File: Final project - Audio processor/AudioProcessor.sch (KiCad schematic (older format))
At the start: 77 parts, among them J1 INPUT STEREO, J2 INPUT MONO STEREO, J3 JCH1, J4 JCH2, J5 ALIMENTACION, J6 JCH3, J7 OUTPUT STEREO, J8 OUTPUT MONO STEREO, J9 I2C & RS232 CONNECTOR, Q1 Q_NPN_BCE, Q2 Q, Q3 Q_NPN_BCE, Q4 Q_NPN_BCE, U1 LM2904, U2 LM2904, U3 pcm5100

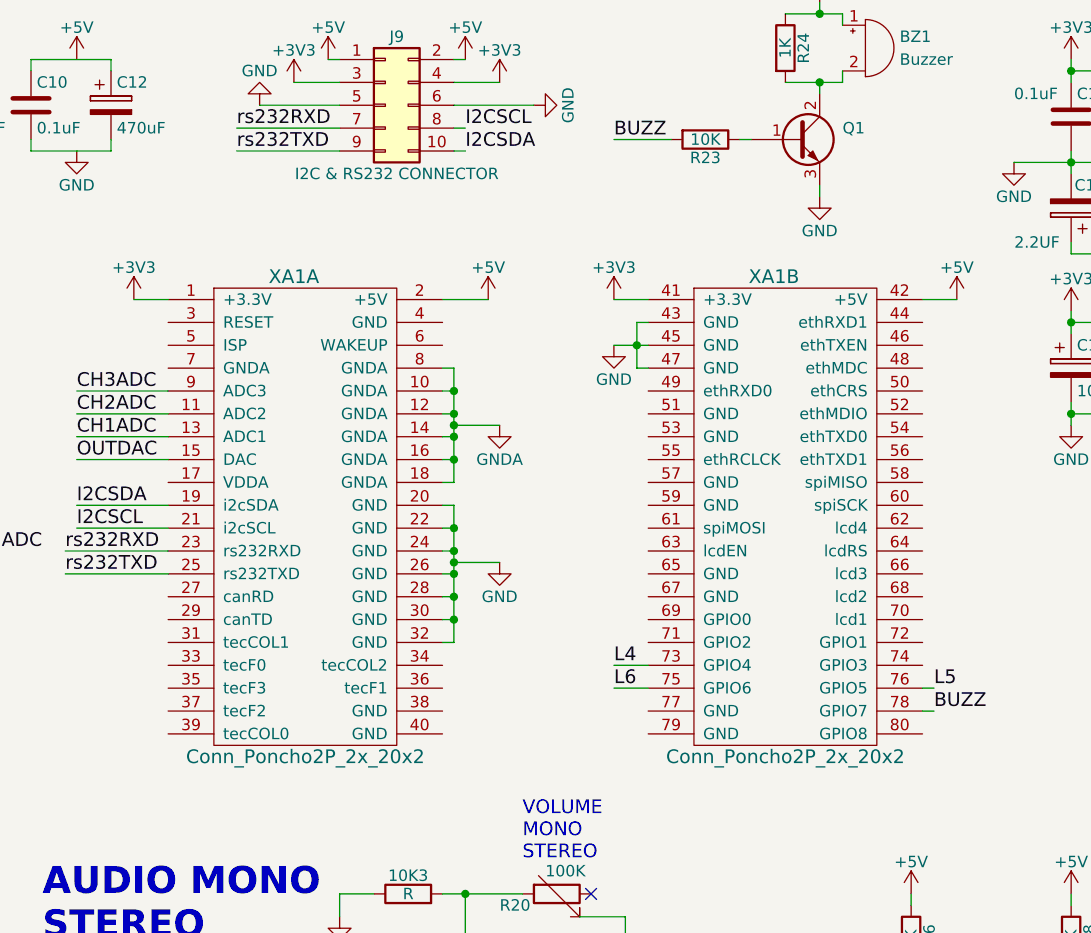
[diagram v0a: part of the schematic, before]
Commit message: Se actualiza el esquematico
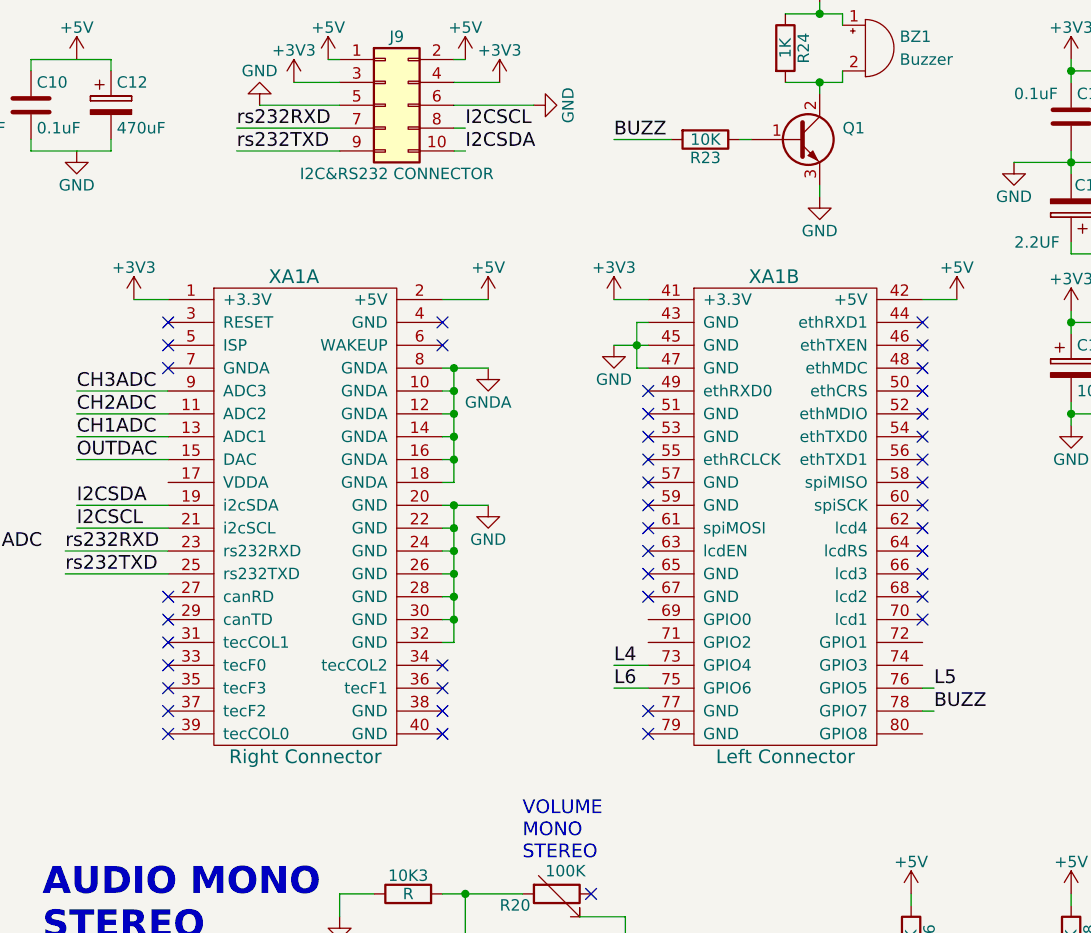
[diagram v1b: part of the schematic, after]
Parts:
- J9: value I2C & RS232 CONNECTOR -> I2C&RS232 CONNECTOR
- XA1: value Conn_Poncho2P_2x_20x2 -> Right Connector
- XA1: value Conn_Poncho2P_2x_20x2 -> Left Connector
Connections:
- no-connect marks 3 -> 45
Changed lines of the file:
@@
 P 4600 2400
 F 0 "XA1" H 4900 2800 60  0000 C CNN
-F 1 "Conn_Poncho2P_2x_20x2" H 4950 700 60  0000 C CNN
+F 1 "Right Connector" H 4950 700 60  0000 C CNN
 F 2 "" H 4600 2400 60  0000 C CNN
 F 3 "" H 4600 2400 60  0000 C CNN
@@
 P 6700 2400
 F 0 "XA1" H 7000 2800 60  0000 C CNN
-F 1 "Conn_Poncho2P_2x_20x2" H 7050 700 60  0000 C CNN
+F 1 "Left Connector" H 7050 700 60  0000 C CNN
 F 2 "" H 6700 2400 60  0000 C CNN
 F 3 "" H 6700 2400 60  0000 C CNN
@@
 L GNDA #PWR36
 U 1 1 5BA0895E
-P 5800 2650
-F 0 "#PWR36" H 5800 2400 50  0001 C CNN
-F 1 "GNDA" H 5800 2500 50  0000 C CNN
-F 2 "" H 5800 2650 50  0001 C CNN
-F 3 "" H 5800 2650 50  0001 C CNN
-	1    5800 2650
+P 5750 2400
+F 0 "#PWR36" H 5750 2150 50  0001 C CNN
+F 1 "GNDA" H 5750 2250 50  0000 C CNN
+F 2 "" H 5750 2400 50  0001 C CNN
+F 3 "" H 5750 2400 50  0001 C CNN
+	1    5750 2400
 	1    0    0    -1
 $EndComp
@@
 L GND #PWR37
 U 1 1 5BA0ECD7
-P 5800 3250
-F 0 "#PWR37" H 5800 3000 50  0001 C CNN
-F 1 "GND" H 5800 3100 50  0000 C CNN
-F 2 "" H 5800 3250 50  0001 C CNN
-F 3 "" H 5800 3250 50  0001 C CNN
-	1    5800 3250
+P 5750 3000
+F 0 "#PWR37" H 5750 2750 50  0001 C CNN
+F 1 "GND" H 5750 2850 50  0000 C CNN
+F 2 "" H 5750 3000 50  0001 C CNN
+F 3 "" H 5750 3000 50  0001 C CNN
+	1    5750 3000
 	1    0    0    -1
 $EndComp
@@
 $EndComp
 Wire Wire Line
-	5550 3000 5600 3000
+	5550 3000 5750 3000
 Wire Wire Line
 	5600 3000 5600 3600
@@
 	5550 3100 5600 3100
 Connection ~ 5600 3100
-Wire Wire Line
-	5800 3250 5600 3250
-Connection ~ 5600 3250
 Wire Wire Line
 	6450 2300 6300 2300
@@
 	3950 3100 4350 3100
 Wire Wire Line
-	5600 2400 5550 2400
+	5550 2400 5750 2400
 Connection ~ 5600 2500
 $Comp
@@
 P 5300 1250
 F 0 "J9" H 5350 1550 50  0000 C CNN
-F 1 "I2C & RS232 CONNECTOR" H 5350 950 50  0000 C CNN
+F 1 "I2C&RS232 CONNECTOR" H 5350 950 50  0000 C CNN
 F 2 "" H 5300 1250 50  0001 C CNN
 F 3 "" H 5300 1250 50  0001 C CNN
@@
 Wire Wire Line
 	5550 2700 5600 2700
-Wire Wire Line
-	5600 2650 5800 2650
-Connection ~ 5600 2650
 Text Label 6300 1400 0    60   ~ 0
 BUZZ
@@
 	7200 800  7200 850
 Connection ~ 7200 850
+NoConn ~ 4350 3400
+NoConn ~ 4350 3500
+NoConn ~ 4350 3600
+NoConn ~ 4350 3700
+NoConn ~ 4350 3800
+NoConn ~ 4350 3900
+NoConn ~ 4350 4000
+NoConn ~ 5550 3800
+NoConn ~ 5550 3700
+NoConn ~ 5550 4000
+NoConn ~ 5550 3900
+NoConn ~ 7650 2600
+NoConn ~ 7650 2200
+NoConn ~ 7650 2300
+NoConn ~ 7650 2400
+NoConn ~ 7650 2500
+NoConn ~ 7650 2700
+NoConn ~ 7650 2800
+NoConn ~ 7650 2900
+NoConn ~ 7650 3000
+NoConn ~ 6450 2500
+NoConn ~ 6450 2600
+NoConn ~ 6450 2700
+NoConn ~ 6450 2800
+NoConn ~ 6450 2900
+NoConn ~ 6450 3000
+NoConn ~ 6450 3100
+NoConn ~ 6450 3200
+NoConn ~ 7650 3100
+NoConn ~ 7650 3200
+NoConn ~ 7650 3300
+NoConn ~ 7650 3400
+NoConn ~ 7650 3500
+NoConn ~ 6450 3300
+NoConn ~ 6450 3400
+NoConn ~ 6450 3900
+NoConn ~ 6450 4000
+NoConn ~ 5550 2200
+NoConn ~ 5550 2300
+Connection ~ 5600 2400
+Connection ~ 5600 3000
+NoConn ~ 4350 2400
+NoConn ~ 4350 2300
+NoConn ~ 4350 2200
 $EndSCHEMATC

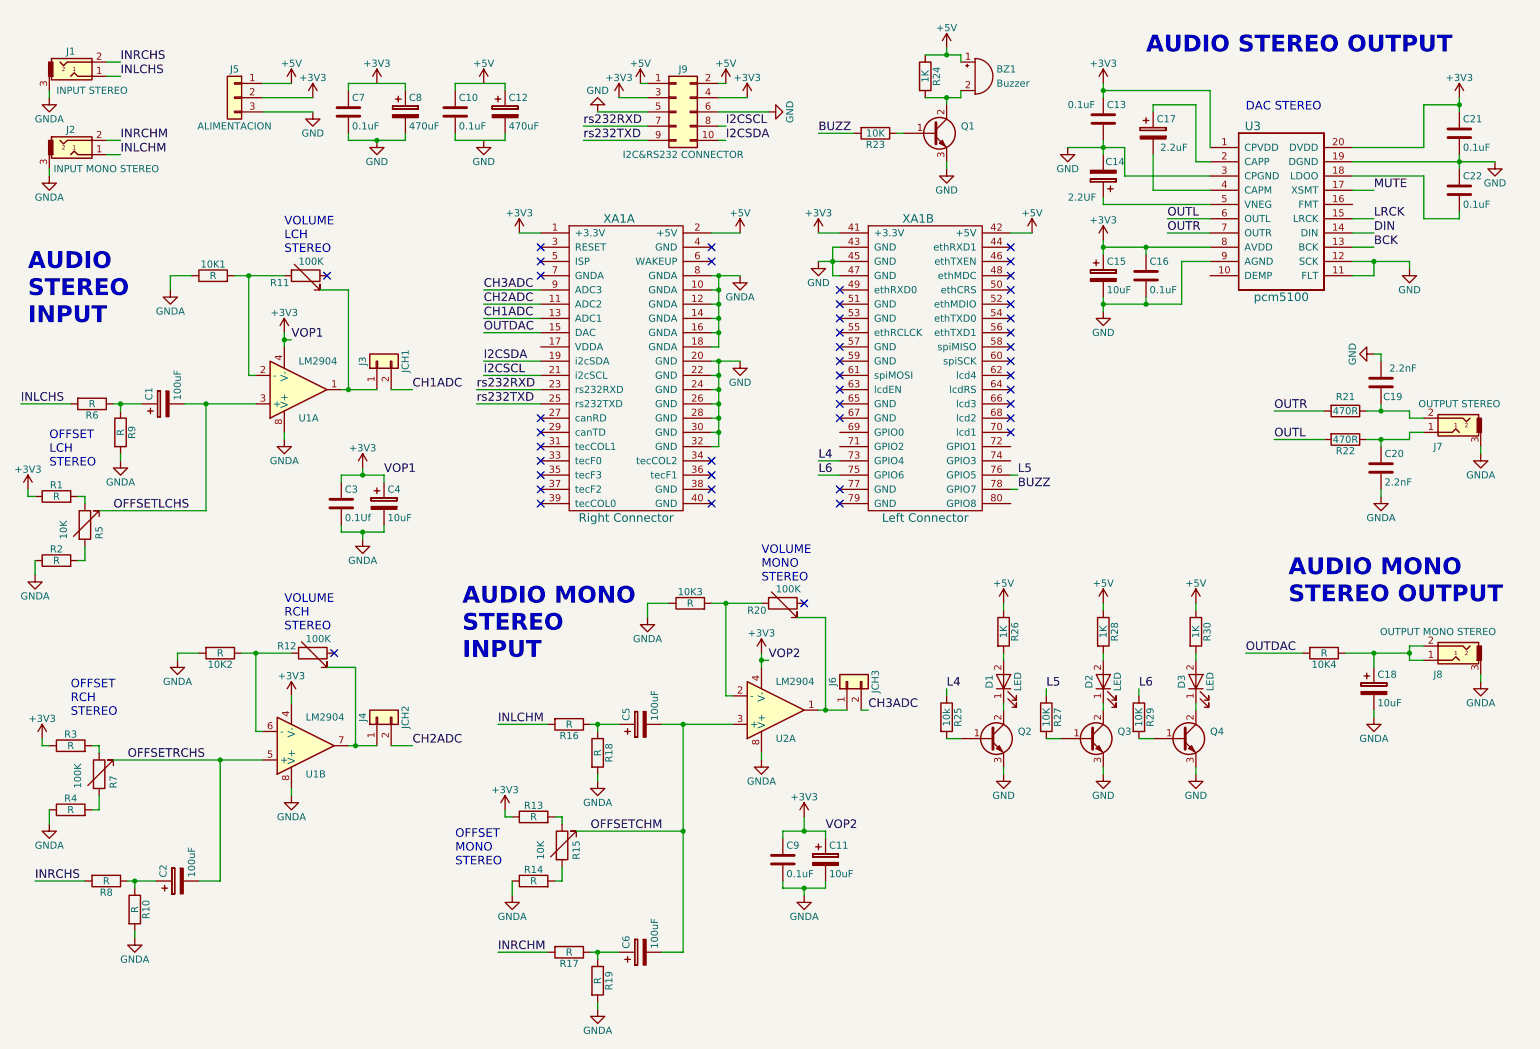
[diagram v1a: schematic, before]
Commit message: Se actualizo el esquematico
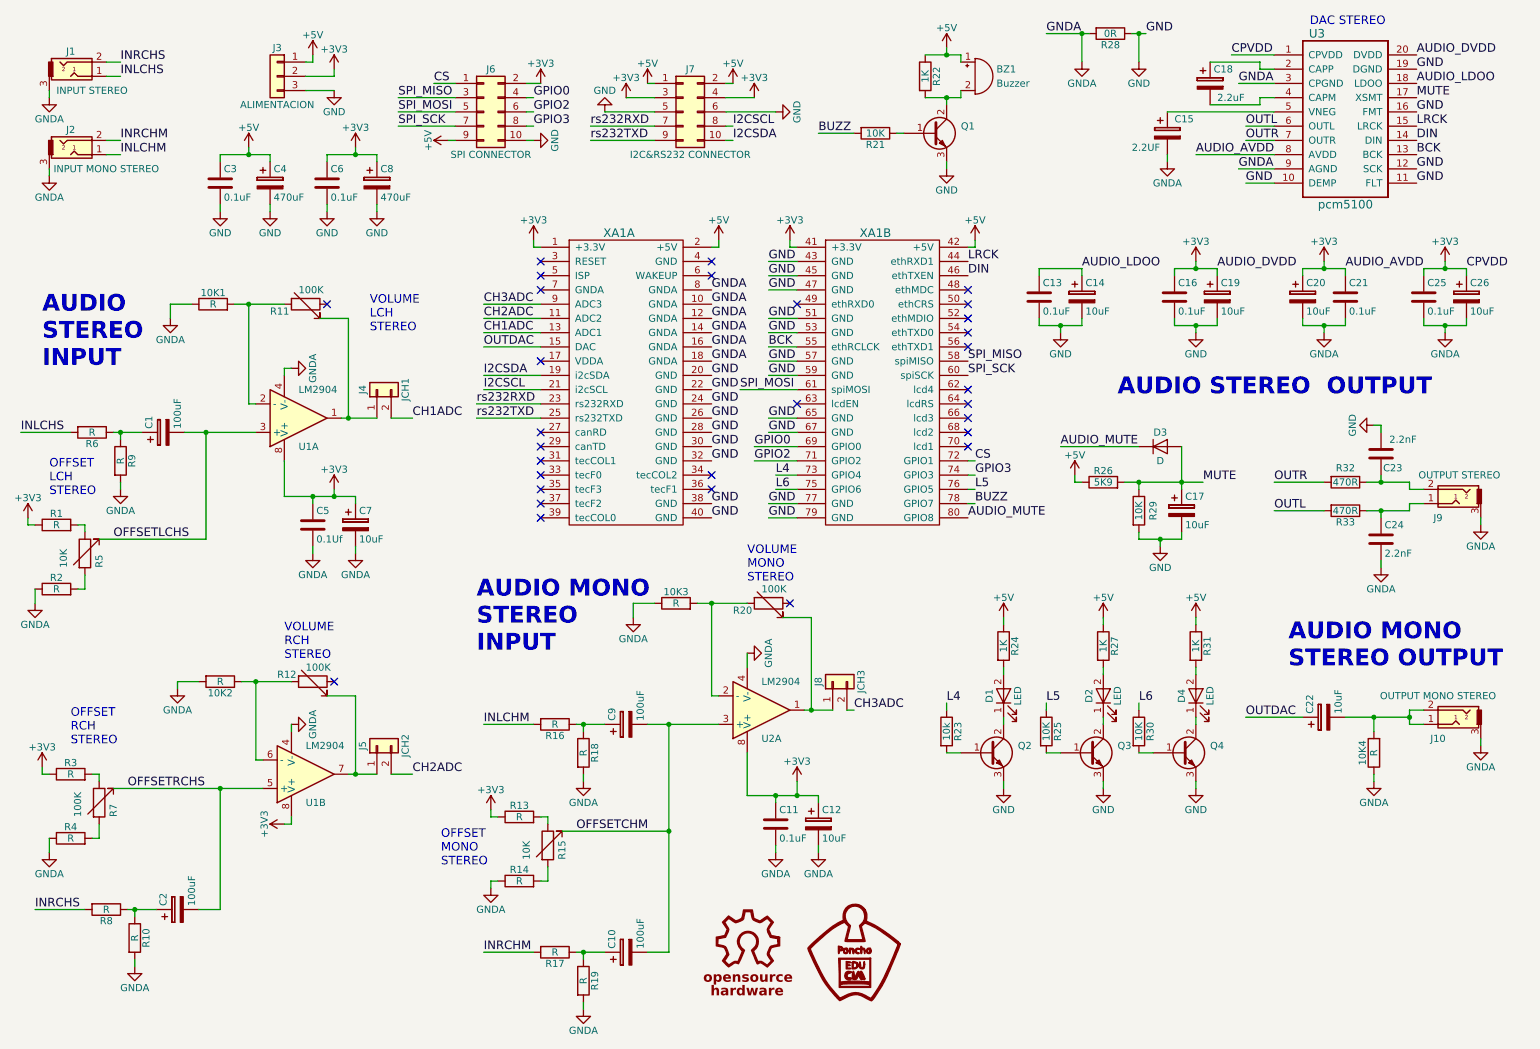
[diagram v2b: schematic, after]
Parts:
- removed C13: 0.1uF, symbol C
- added C14, C17, C19, C26: 10uF, symbol CP
- added C25: 0.1uF, symbol C
- added D3: D, symbol D
- added J6: SPI CONNECTOR, symbol Conn_02x05_Odd_Even
- added R26: 5K9, symbol R
- added R28: 0R, symbol R
- added R29: 10K, symbol R
- XA1: value Right Connector -> Conn_Poncho2P_2x_20x2
- XA1: value Left Connector -> Conn_Poncho2P_2x_20x2
- renumbered C6 to C10, C9 to C11, C11 to C12, C22 to C13, C14 to C15, C21 to C16, C17 to C18, C15 to C20, C16 to C21, C18 to C22, C19 to C23, C20 to C24, C10 to C3, C12 to C4, C3 to C5, C7 to C6, C4 to C7, C5 to C9, D3 to D4, J8 to J10, J5 to J3, J3 to J4, J4 to J5, J9 to J7, J6 to J8, J7 to J9, R23 to R21, R24 to R22, R25 to R23, R26 to R24, R27 to R25, R28 to R27, R29 to R30, R30 to R31, R21 to R32, R22 to R33
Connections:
- net +3V3: now also C6.1, C8.1, U1.8 (V+), U1.8 (V+), U2.8 (V+), C19.1, C25.1, C26.1, J6.2 (Pin_2); no longer U1.4 (V-), U1.4 (V-), U2.4 (V-)
- net +5V: now also C3.1, C4.1, J6.9 (Pin_9), R26.1
- net BCK: now also XA1.55 (ethRCLCK)
- net DIN: now also XA1.46 (ethTXEN)
- net GND: now also C13.2, C3.2, C4.2, U3.10 (DEMP), U3.16 (FMT), XA1.38 (GND), XA1.40 (GND), XA1.51 (GND), XA1.53 (GND), XA1.57 (GND), XA1.59 (GND), XA1.65 (GND), XA1.67 (GND), XA1.77 (GND), XA1.79 (GND), C14.2, C17.2, C19.2, J6.10 (Pin_10), R28.1, R29.2; no longer C13.1, C15.2, C20.2, C21.2, U3.3 (CPGND), U3.9 (AGND)
- net GNDA: now also 10K4.1, C15.2, C20.2, C21.2, U1.4 (V-), U1.4 (V-), U2.4 (V-), U3.3 (CPGND), U3.9 (AGND), C25.2, C26.2, R28.2; no longer C22.2, U1.8 (V+), U1.8 (V+), U2.8 (V+)
- net LRCK: now also XA1.44 (ethRXD1)
- net MUTE: now also C17.1, D3.2 (A), R26.2, R29.1
- net OUTDAC: now also C22.1; no longer 10K4.2
- net AUDIO_LDOO: now reaches U3.18 (LDOO)
- net AUDIO_LDOO: now also C13.1, C14.1; no longer C13.2
- net at J10.1, J10.2: now also 10K4.2, C22.2; no longer 10K4.1, C22.1
- net SPI_MISO: now reaches XA1.58 (spiMISO)
- net SPI_MISO: now also J6.3 (Pin_3)
- net SPI_SCK: now reaches XA1.60 (spiSCK)
- net SPI_SCK: now also J6.7 (Pin_7)
- net SPI_MOSI: now reaches XA1.61 (spiMOSI)
- net SPI_MOSI: now also J6.5 (Pin_5)
- net GPIO0: now reaches XA1.69 (GPIO0)
- net GPIO0: now also J6.4 (Pin_4)
- net GPIO2: now reaches XA1.71 (GPIO2)
- net GPIO2: now also J6.6 (Pin_6)
- net CS: now reaches XA1.72 (GPIO1)
- net CS: now also J6.1 (Pin_1)
- net GPIO3: now reaches XA1.74 (GPIO3)
- net GPIO3: now also J6.8 (Pin_8)
- net AUDIO_MUTE: now reaches XA1.80 (GPIO8)
- net AUDIO_MUTE: now also D3.1 (K)
- no-connect marks 45 -> 30
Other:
- moved on the sheet: 10K1, 10K2, 10K3, 10K4, C1, C10, C11, C12, C13, C15, C16, C18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

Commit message: Actualizacion repo
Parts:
- BZ1: footprint (none) -> Buzzers_Beepers:Buzzer_12x9.5RM7.6
- C1, C10, C2, C9: footprint (none) -> Capacitors_SMD:CP_Elec_6.3x5.3
- C11, C13, C16, C21, C23, C24, C25, C3, C5, C6: footprint (none) -> Capacitors_SMD:C_1206_HandSoldering
- C12, C14, C17, C19, C20, C22, C26, C7: footprint (none) -> Capacitors_SMD:CP_Elec_5x5.3
- C15, C18: footprint (none) -> Capacitors_THT:CP_Radial_D5.0mm_P2.50mm
- C4, C8: footprint (none) -> Capacitors_THT:CP_Radial_D10.0mm_P5.00mm
- D1, D2, D4: footprint (none) -> LEDs:LED_1206_HandSoldering
- D3: value D -> 1N4148; footprint (none) -> Diodes_SMD:D_1206
- J1, J10, J2, J9: footprint (none) -> Connectors:BARREL_JACK
- J3: footprint (none) -> TerminalBlocks_Phoenix:TerminalBlock_Phoenix_MKDS1.5-3pol
- J4, J5, J8: footprint (none) -> Pin_Headers:Pin_Header_Straight_1x02_Pitch2.54mm
- J6: value SPI CONNECTOR -> SPI & I/0; footprint (none) -> Socket_Strips:Socket_Strip_Straight_2x05_Pitch2.54mm
- J7: value I2C&RS232 CONNECTOR -> I2C & RS232; footprint (none) -> Socket_Strips:Socket_Strip_Straight_2x05_Pitch2.54mm
- Q1, Q2, Q3, Q4: footprint (none) -> TO_SOT_Packages_THT:TO-92_Molded_Narrow
- R1, R13, R14, R2, R3, R4: value R -> 1K; footprint (none) -> Resistors_SMD:R_1206_HandSoldering
- R10, R16, R17, R18, R19, R6, R8, R9: value R -> 10K; footprint (none) -> Resistors_SMD:R_2010_HandSoldering
- R11, R12, R15, R20, R5: footprint (none) -> Potentiometers:Potentiometer_Trimmer_Bourns_3296W
- R21, R23, R25, R29, R30: footprint (none) -> Resistors_SMD:R_2010_HandSoldering
- R22, R24, R26, R27, R28, R31, R32, R33: footprint (none) -> Resistors_SMD:R_1206_HandSoldering
- R34: renamed from 10K1; value R -> 10K; footprint (none) -> Resistors_SMD:R_2010_HandSoldering
- R35: renamed from 10K2; value R -> 10K; footprint (none) -> Resistors_SMD:R_2010_HandSoldering
- R36: renamed from 10K3; value R -> 10K; footprint (none) -> Resistors_SMD:R_2010_HandSoldering
- R37: renamed from 10K4; value R -> 10K; footprint (none) -> Resistors_SMD:R_2010_HandSoldering
- R7: value 100K -> 10K; footprint (none) -> Potentiometers:Potentiometer_Trimmer_Bourns_3296W
- U1, U2: footprint (none) -> Housings_SOIC:SOIC-8_3.9x4.9mm_Pitch1.27mm
- U3: footprint (none) -> Housings_SSOP:TSSOP-20_4.4x6.5mm_Pitch0.65mm
- XA1: footprint (none) -> Poncho_Esqueleto:Conn_Poncho_Completo
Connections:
- net +3V3: no longer XA1.1 (+3.3V)
- net +5V: no longer XA1.2 (+5V)
- no-connect marks 30 -> 32

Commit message: Se actualiza el PCB, todavia queda rutear un poco.
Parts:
- removed BZ1: Buzzer, Buzzers_Beepers:Buzzer_12x9.5RM7.6, symbol Buzzer
- removed Q1: Q_NPN_BCE, TO_SOT_Packages_THT:TO-92_Molded_Narrow, symbol Q_NPN_BCE
- removed R21: 10K, Resistors_SMD:R_2010_HandSoldering, symbol R
- removed R22: 1K, Resistors_SMD:R_1206_HandSoldering, symbol R
- R11, R12, R15, R20, R5, R7: symbol R_Variable -> R_Variable-RESCUE-AudioProcessor
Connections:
- net BUZZ: no longer names the net of XA1.78 (GPIO7)
- no-connect marks 32 -> 33
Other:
- moved on the sheet: J6, J7, R28

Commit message: avanzando con el pcb
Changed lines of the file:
@@
 	7850 2400 7850 2350
 Wire Wire Line
-	8150 2350 8150 2400
-Text Label 8150 2350 0    60   ~ 0
+	8150 2250 8150 2400
+Text Label 8150 2250 0    60   ~ 0
 AUDIO_LDOO
 Text Label 10500 950  0    60   ~ 0
@@
 	8800 2350 9100 2350
 Wire Wire Line
-	9100 2350 9100 2400
+	9100 2250 9100 2400
 Wire Wire Line
 	8800 2700 8800 2750
@@
 	8950 2300 8950 2350
 Connection ~ 8950 2350
-Text Label 9100 2350 0    60   ~ 0
+Text Label 9100 2250 0    60   ~ 0
 AUDIO_DVDD
 Wire Wire Line
@@
 	9700 2350 10000 2350
 Wire Wire Line
-	10000 2350 10000 2400
+	10000 2250 10000 2400
 Wire Wire Line
 	9850 2300 9850 2350
@@
 Text Label 8950 1550 0    60   ~ 0
 AUDIO_AVDD
-Text Label 10000 2350 0    60   ~ 0
+Text Label 10000 2250 0    60   ~ 0
 AUDIO_AVDD
 Text Label 9250 1650 0    60   ~ 0
@@
 	10550 2350 10850 2350
 Wire Wire Line
-	10850 2350 10850 2400
+	10850 2250 10850 2400
 Wire Wire Line
 	10700 2300 10700 2350
@@
 Wire Wire Line
 	9500 850  9200 850
-Text Label 10850 2350 0    60   ~ 0
+Text Label 10850 2250 0    60   ~ 0
 CPVDD
 $Comp
@@
 	5900 1250 6100 1250
 NoConn ~ 7400 4000
+Connection ~ 9100 2350
+Connection ~ 8150 2350
+Connection ~ 10000 2350
+Connection ~ 10850 2350
 $EndSCHEMATC

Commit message: Version 2 del pcb del procesador de audio
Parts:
- D3: footprint Diodes_SMD:D_1206 -> Diodes_THT:D_A-405_P10.16mm_Horizontal
- R32, R33: footprint Resistors_SMD:R_1206_HandSoldering -> Resistors_THT:R_Axial_DIN0207_L6.3mm_D2.5mm_P10.16mm_Horizontal
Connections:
- net AUDIO_LDOO: no longer names the net of C13.1, C14.1, U3.18 (LDOO)
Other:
- note added: "AUDIO STEREO \nOUTPUT\n"
- note removed: "AUDIO STEREO OUTPUT\n"
- moved on the sheet: C13, C14, C15, C16, C17, C18, C19, C20, C21, C25, C26, D3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

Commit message: version Final
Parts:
- J1, J10, J2, J9: footprint Connectors:BARREL_JACK -> plug3:plug3.5mmAudio
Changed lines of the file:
@@
 LIBS:contrib
 LIBS:valves
+LIBS:AudioProcessor-cache
 LIBS:poncho_grande-cache
-LIBS:AudioProcessor-cache
 EELAYER 25 0
 EELAYER END
@@
 F 0 "J9" H 10850 3900 50  0000 C CNN
 F 1 "OUTPUT STEREO" H 10700 4200 50  0000 C CNN
-F 2 "Connectors:BARREL_JACK" H 11000 4100 50  0001 C CNN
+F 2 "plug3:plug3.5mmAudio" H 11000 4100 50  0001 C CNN
 F 3 "" H 11000 4100 50  0001 C CNN
 	1    10750 4000
@@
 F 0 "J1" H 1050 1175 50  0000 C CNN
 F 1 "INPUT STEREO" H 1200 900 50  0000 C CNN
-F 2 "Connectors:BARREL_JACK" H 1350 1100 50  0001 C CNN
+F 2 "plug3:plug3.5mmAudio" H 1350 1100 50  0001 C CNN
 F 3 "" H 1350 1100 50  0001 C CNN
 	1    1100 1000
@@
 F 0 "J2" H 1050 1725 50  0000 C CNN
 F 1 "INPUT MONO STEREO" H 1300 1450 50  0000 C CNN
-F 2 "Connectors:BARREL_JACK" H 1350 1650 50  0001 C CNN
+F 2 "plug3:plug3.5mmAudio" H 1350 1650 50  0001 C CNN
 F 3 "" H 1350 1650 50  0001 C CNN
 	1    1100 1550
@@
 F 0 "J10" H 10850 5450 50  0000 C CNN
 F 1 "OUTPUT MONO STEREO" H 10850 5750 50  0000 C CNN
-F 2 "Connectors:BARREL_JACK" H 11000 5650 50  0001 C CNN
+F 2 "plug3:plug3.5mmAudio" H 11000 5650 50  0001 C CNN
 F 3 "" H 11000 5650 50  0001 C CNN
 	1    10750 5550
